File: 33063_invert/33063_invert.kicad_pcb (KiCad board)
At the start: 2 copper layers, 47 x 20 mm, 14 parts, among them J1 Conn_01x02, J2 Conn_01x02, U1 33063

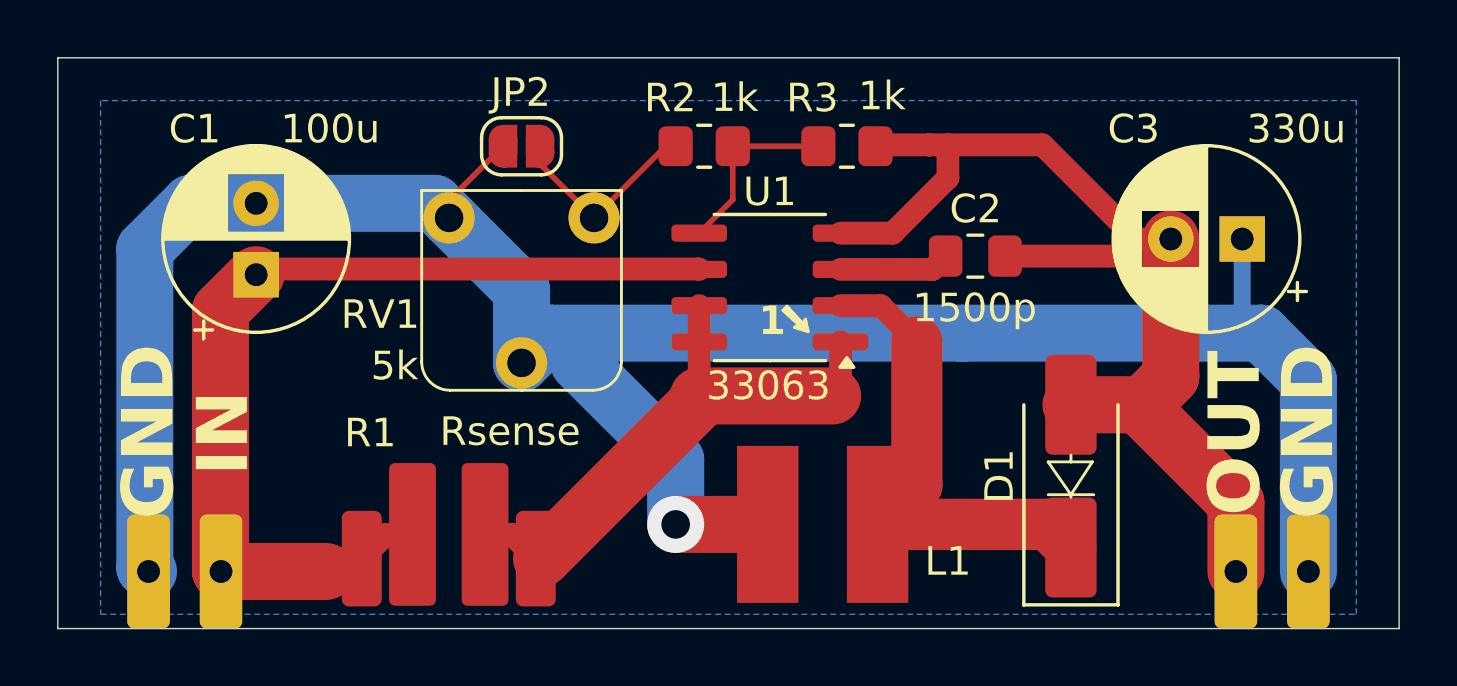
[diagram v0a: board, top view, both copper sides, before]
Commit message: added DFN breakout changed trim pot type in 33063_boost, 33063_invert, r1283_power boards fixed error in 33063_boost board (move trim pot to higher side of voltage divider)
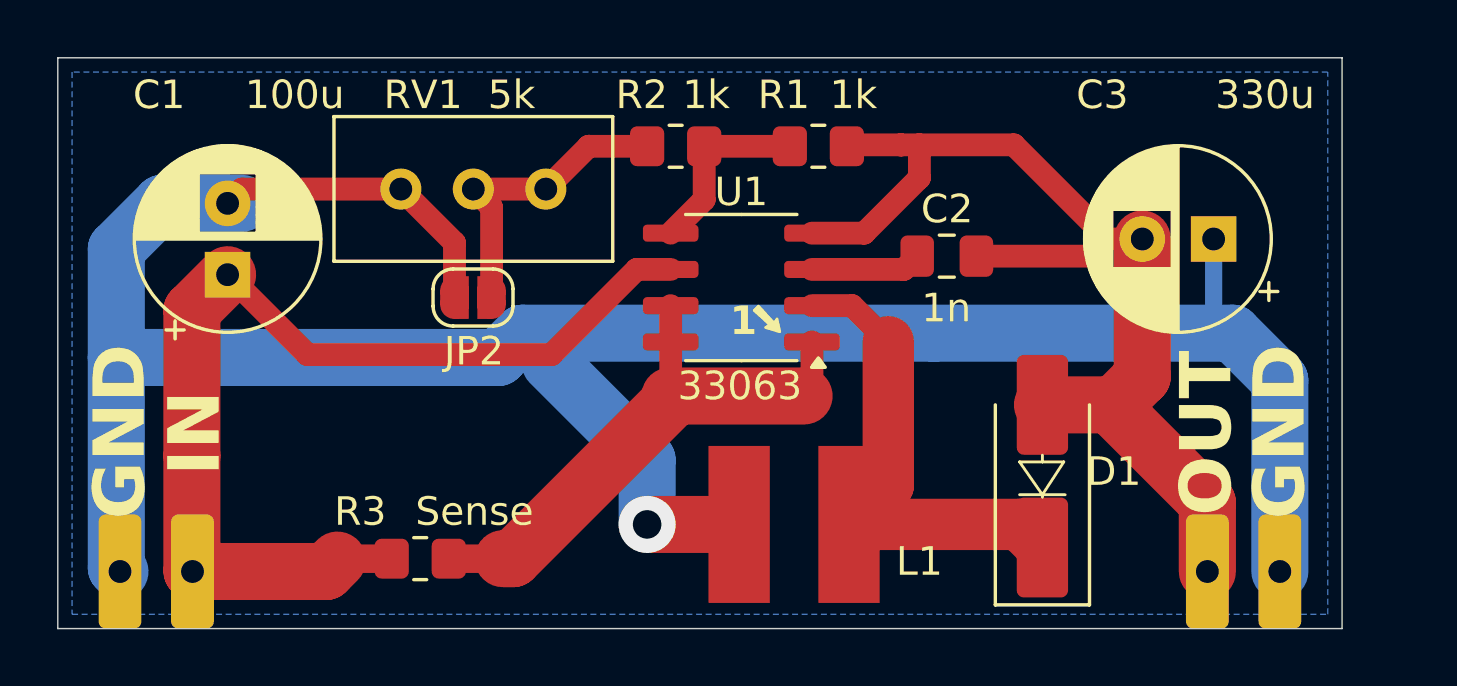
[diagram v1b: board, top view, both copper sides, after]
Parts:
- removed R100: 1, misc:0805_5mm
- C2: value 1500p -> 1n
- R3: renamed from R1; value Rsense -> Sense; footprint Resistor_SMD:R_2512_6332Metric_Pad1.40x3.35mm_HandSolder -> Resistor_SMD:R_0805_2012Metric_Pad1.20x1.40mm_HandSolder
- RV1: footprint misc:trim_pot -> Potentiometer_THT:Potentiometer_Bourns_3296W_Vertical
- moved JP2 5.57 mm to (64.5, 58.4), turned to 180 degrees
- moved RV1 5.52 mm to (62.0, 54.6)
- moved C1 1.00 mm to (56.0, 57.6)
- moved C2 1.00 mm to (81.2, 57.0)
- moved C3 1.00 mm to (90.5, 56.4)
- moved D1 1.00 mm to (84.5, 64.7)
- moved J1 1.00 mm to (53.5, 70.0)
- moved J2 1.00 mm to (91.5, 70.0)
- moved L1 1.00 mm to (75.8, 66.3)
- moved R1 1.00 mm to (76.7, 53.1)
- moved R2 1.00 mm to (71.7, 53.1)
- moved R3 1.00 mm to (62.7, 67.5)
- moved U1 1.00 mm to (74.0, 58.0)
- renumbered R3 to R1
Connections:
- C1 pad 2: GND2 -> GND
- C3 pad 1: GND2 -> GND
- J1 pad 1: GND2 -> GND
- J2 pad 2: GND2 -> GND
- JP2 pad 1: GND2 -> Net-(JP2-A)
- JP2 pad 2: Net-(JP2-B) -> GND
- L1 pad 1: GND2 -> GND
- R2 pad 1: Net-(JP2-B) -> Net-(JP2-A)
- RV1 pad 1: Net-(JP2-B) -> GND
- RV1 pad 2: GND2 -> Net-(JP2-A)
- RV1 pad 3: GND2 -> Net-(JP2-A)
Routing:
- net GND: track 0.00 -> 91.1 mm, vias 0 -> 1
- net GND2: track 83.8 -> 0.00 mm, vias 1 -> 0
- net Net-(JP2-A): track 0.00 -> 10.8 mm
- net Net-(JP2-B): track 7.19 -> 0.00 mm
- net /Vin_2: track 33.8 -> 36.0 mm
- added copper zone on B.Cu, net GND
- removed copper zone on B.Cu, net GND2
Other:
- board size 47 x 20 mm -> 45 x 20 mm
- board text added: "Vout = -1.25 * (1 + (R2+RV1) / R1)"
- board text removed: "Vout = -1.25 * (1 + R8 / R7)"
